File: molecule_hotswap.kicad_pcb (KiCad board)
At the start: 2 copper layers, 18.3 x 14.2 mm, 6 parts, among them J1 kailh_hotswap_mx, P1 MountingHole_Pad, P2 MountingHole_Pad

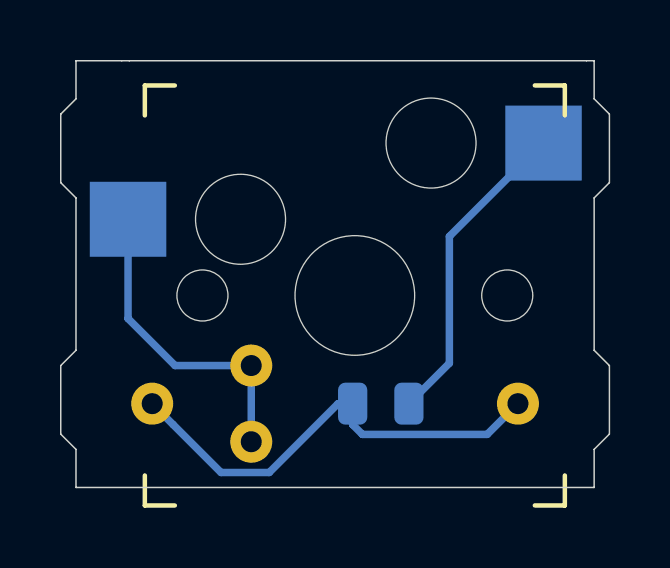
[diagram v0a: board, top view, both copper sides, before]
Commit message: moved holes to the edges and added a redundant column hole
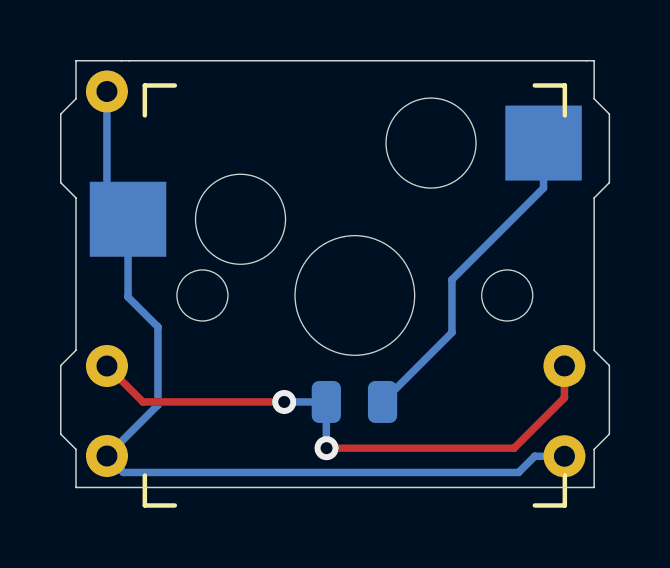
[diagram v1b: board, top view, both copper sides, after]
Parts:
- added SC: MountingHole_Pad, Connector_Pin:Pin_D0.7mm_L6.5mm_W1.8mm_FlatFork, B.Cu at (141.2, 113.3)
- moved SC 10.3 mm to (126.0, 101.1)
- moved SC 4.83 mm to (126.0, 113.2)
- moved SR 2.00 mm to (141.2, 110.2)
- moved SR 1.96 mm to (126.0, 110.2)
- moved D1 0.88 mm to (134.2, 111.5)
- renumbered P2 to SC, P1 to SC, O2 to SR, O1 to SR
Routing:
- net Net-(J1-Pad2): track 10.6 -> 29.3 mm
- net Net-(D1-Pad1): track 15.4 -> 19.0 mm, vias 0 -> 2
